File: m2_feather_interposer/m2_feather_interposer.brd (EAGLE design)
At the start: 160 x 186.6 mm, 43 parts, among them U1 MAX17043, U2 BQ24195, U3 XCL223

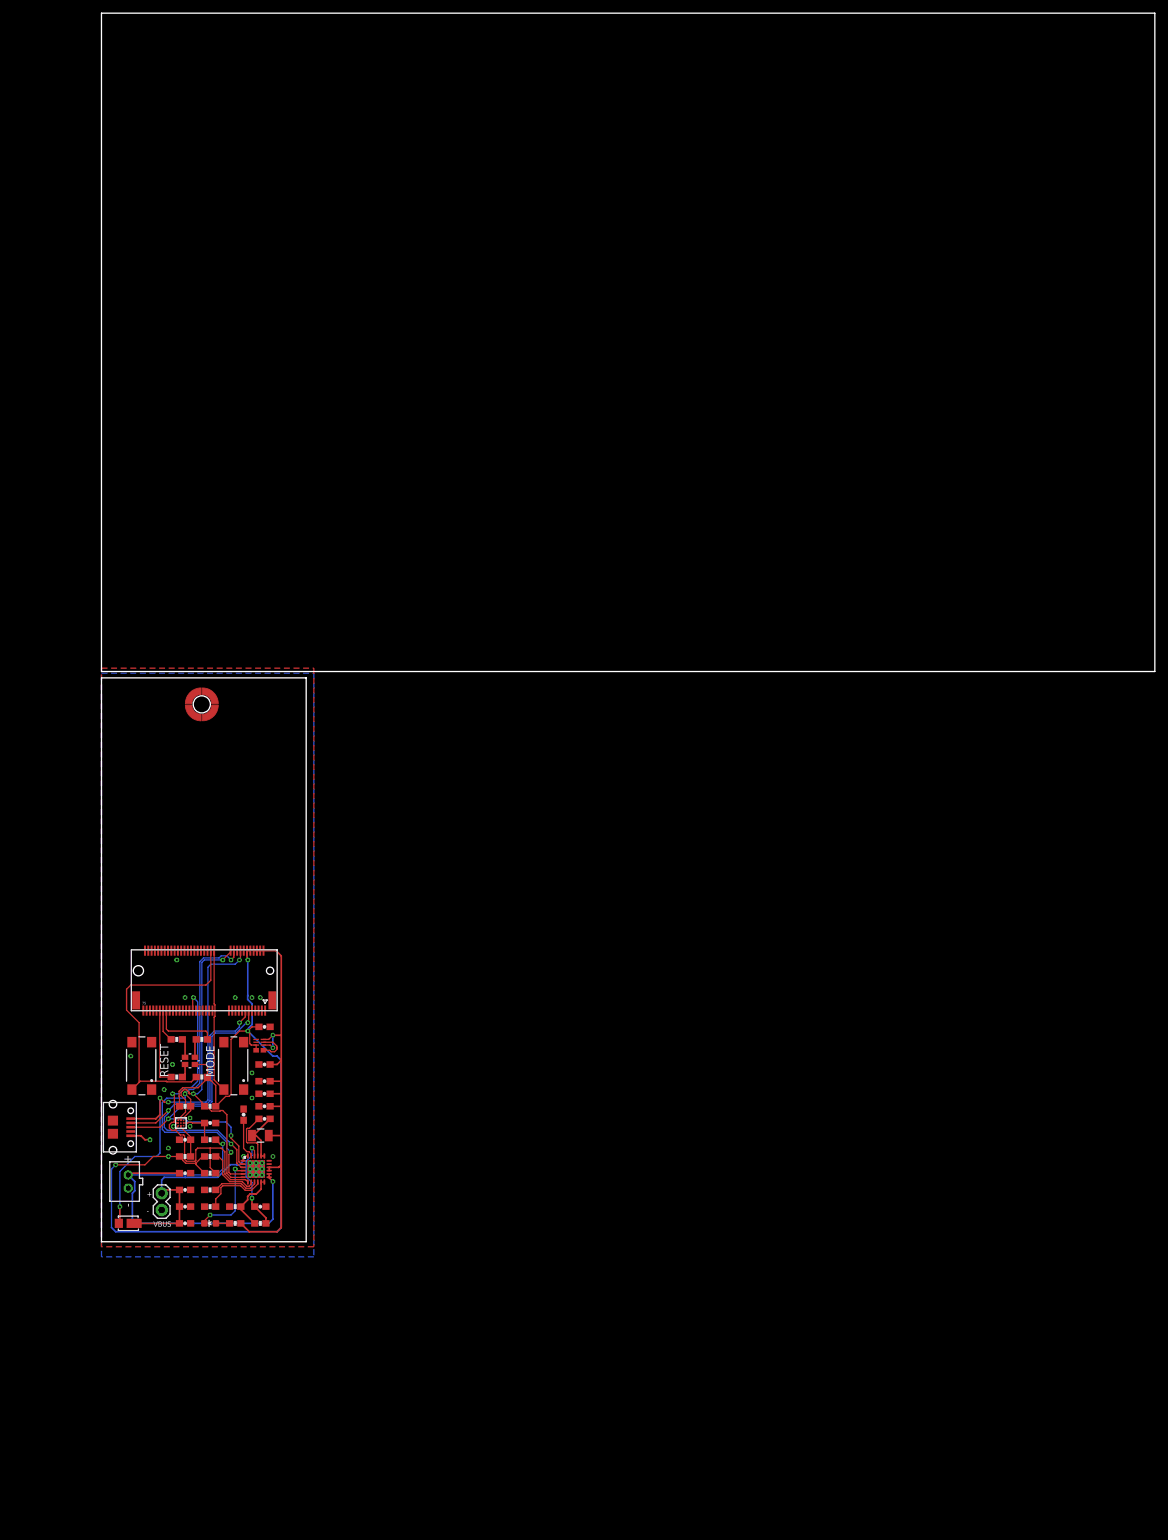
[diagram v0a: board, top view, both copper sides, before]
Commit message: added a whole bunch of stuff, board layout, draft key component placements, added connectors, added components from the boron that were missing.
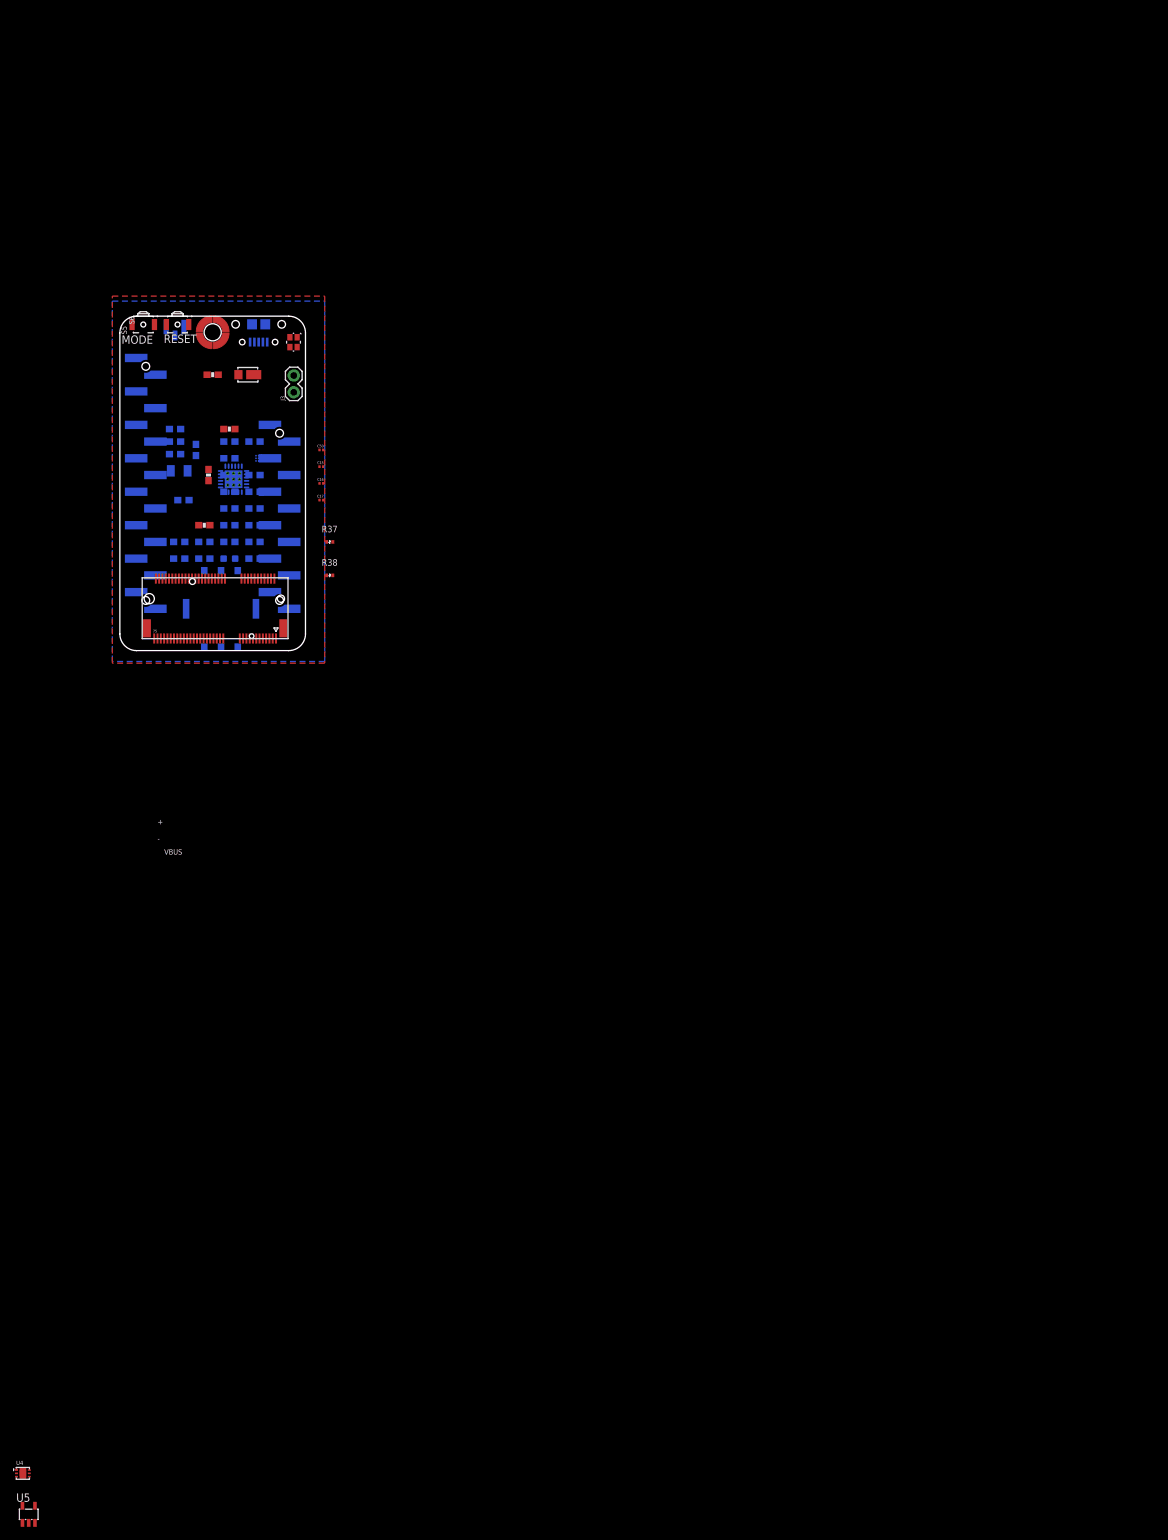
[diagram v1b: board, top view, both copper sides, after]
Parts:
- removed C13: 4.7uF, rickk2:0603-CAP
- removed C14: 10uF, rickk2:0603-CAP
- removed CN1: (no value), rickk2:JST-PH-2-THM
- removed JP1: M02PTH, rickk2:1X02
- removed S1, S2: SWITCH-MOM-4.5, rickk2:SWITCH-MOM-4.5
- removed U3: XCL223, rickk2:REG-XCL223-LESS-CREAM
- added C15, C16, C17: 47pF, m2_feather_interposer:PARTICLE_C0201_B
- added C50: 100nF, m2_feather_interposer:PARTICLE_C0201_B
- added J3: (no value), SparkFun-Connectors:1X02
- added MS1: MICROBUILDER_FEATHERWINGSMT_BTM_FEATHER, m2_feather_interposer:SMT_BTM_FEATHERWING
- added NFC: UFL, m2_feather_interposer:PARTICLE_IPEX-20279-001E
- added R37, R38: ESD NC, m2_feather_interposer:REDBEAR_R-0402S
- added S5, S6: B3U-3000P-B, m2_feather_interposer:SW_B3U-3000P-B
- added U$4: M2_FEATHER_INTERPOSER_PARTICLE_SIM-NANO-4FF, m2_feather_interposer:M2_FEATHER_INTERPOSER_PARTICLE_GCT-SIM8100
- added U4: PARTICLE_XC9258A33EER-G, m2_feather_interposer:PARTICLE_USP-6C
- added U5: PARTICLE_XC8107SOT25, m2_feather_interposer:PARTICLE_SOT25
- C1, C10, C11, C12, C4, C5, C6, C7, C8, C9: device rickk2:0603-CAP -> m2_feather_interposer:RICKK2_0603-CAP
- D1: device rickk2:LED-0603 -> m2_feather_interposer:RICKK2_LED-0603
- D2: device rickk2:SOD-123HE-ON -> m2_feather_interposer:RICKK2_SOD-123HE-ON
- J1: value (none) -> RICKK2_SPARK_M.2EKEY; device rickk2:SPARK_M.2EKEY-LESS-CREAM -> m2_feather_interposer:RICKK2_SPARK_M.2EKEY-LESS-CREAM
- L1: device rickk2:1008-BOURNS -> m2_feather_interposer:RICKK2_1008-BOURNS
- LED1: value LED-RGB-CREE-SMD -> RICKK2_LED-RGB-CREE-SMD; device rickk2:LED-RGB-CREE-SMD -> m2_feather_interposer:RICKK2_LED-RGB-CREE-SMD
- R1, R10, R11, R12, R14, R15, R2, R3, R4, R5, R6, R7, R8, R9: device rickk2:0603-RES -> m2_feather_interposer:RICKK2_0603-RES
- U$1: value M2-STANDOFF -> RICKK2_M2-STANDOFF; device rickk2:M2-STANDOFF -> m2_feather_interposer:RICKK2_M2-STANDOFF
- U$3: value USB-MICRO-B-SOCKET-AMPHENOL -> RICKK2_USB-MICRO-B-SOCKET-AMPHENOL; device rickk2:USB-B-SMT-AMPHENOL -> m2_feather_interposer:RICKK2_USB-B-SMT-AMPHENOL
- U1: device rickk2:9UCSP-MAXIM -> m2_feather_interposer:RICKK2_9UCSP-MAXIM
- U2: device rickk2:24VFQN-TI -> m2_feather_interposer:RICKK2_24VFQN-TI
- moved D2 130.2 mm to (22.2, 45.1)
- moved U$3 120.8 mm to (23.9, 50.0), flipped to the bottom, turned to 180 degrees
- moved LED1 110.3 mm to (29.7, 49.3), turned to 90 degrees
- moved U2 104.8 mm to (20.1, 29.2), flipped to the bottom
- moved C10 101.9 mm to (11.2, 36.8), flipped to the bottom
- moved C11 101.9 mm to (11.2, 34.9), flipped to the bottom
- moved C12 101.9 mm to (11.2, 33.0), flipped to the bottom
- moved C8 101.7 mm to (11.8, 19.7), flipped to the bottom
- moved R14 101.7 mm to (11.8, 17.1), flipped to the bottom
- moved U1 101.7 mm to (23.9, 32.4), flipped to the bottom
- moved C1 101.5 mm to (23.2, 29.8), flipped to the bottom
- moved C2 101.5 mm to (23.2, 19.7), flipped to the bottom
- moved C6 101.5 mm to (23.2, 22.2), flipped to the bottom
- moved C7 101.5 mm to (23.2, 24.8), flipped to the bottom
- moved R5 101.5 mm to (23.2, 27.3), flipped to the bottom
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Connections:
- removed net L2: U3.5, U3.8
- new net A0: J1.23, MS1.5
- new net A1: J1.33, MS1.6
- new net A2: J1.35, MS1.7
- new net A3: J1.37, MS1.8
- new net A4: J1.41, MS1.9
- new net A5: J1.43, MS1.10
- new net D2: MS1.19
- new net D3: MS1.20
- new net D4: MS1.21
- new net D5: MS1.22
- new net D6: MS1.23
- new net D7: MS1.24
- new net D8: MS1.25
- new net MISO: J1.50, MS1.13
- new net MOSI: J1.52, MS1.12
- new net NANO_CLK: C16.1
- new net NANO_DATA: C17.1
- new net NANO_RST: C15.1
- new net NANO_VSIM: C50.1
- new net NFC1: NFC.2@1, NFC.2@2, R37.1
- new net NFC2: NFC.1, R38.2
- new net RX: J1.38, MS1.14
- new net SCK: J1.54, MS1.11
- new net SYS_PWR_EN: MS1.27, U5.4
- new net TX: J1.36, MS1.15
- new net VOUT: U4.3, U5.1
- net /MODE: now also MS1.3, S5.2; no longer S1.3
- net /RESET: now also MS1.1, S6.2; no longer S2.3
- net 3V3: now also MS1.2; no longer C14.1, U3.3, U3.7
- net 3V7: now also U4.6; no longer C13.1, U3.4, U3.6
- net BAT: now also J3.1, MS1.28; no longer CN1.1
- net GND: now also C15.2, C16.2, C17.2, C50.2, J3.2, MS1.4, R37.2, R38.1, S5.1, S6.1, U4.2, U4.5, U4.P$1, U5.2; no longer C13.2, C14.2, CN1.2, JP1.2, S1.2, S2.2, U3.1, U3.2
- net SCL: now also MS1.18
- net SDA: now also MS1.17
- net VBUS: now also MS1.26, U5.5; no longer JP1.1
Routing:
- net 3V3: track 135.5 -> 0.00 mm, vias 4 -> 0
- net 3V7: track 70.6 -> 0.00 mm, vias 2 -> 0
- net VUSB: track 65.4 -> 0.00 mm, vias 4 -> 0
- net BAT: track 64.0 -> 0.00 mm, vias 2 -> 0
- net SCL: track 59.7 -> 0.00 mm, vias 3 -> 0
- net BATINT: track 52.4 -> 0.00 mm, vias 2 -> 0
- net SDA: track 51.8 -> 0.00 mm, vias 2 -> 0
- net USB-D-: track 49.7 -> 0.00 mm, vias 3 -> 0
- net USB-D+: track 48.7 -> 0.00 mm, vias 3 -> 0
- net /RESET: track 43.4 -> 0.00 mm
- net VBUS: track 32.6 -> 0.00 mm, vias 1 -> 0
- net /MODE: track 21.8 -> 0.00 mm
- net REGN: track 14.4 -> 0.00 mm, vias 2 -> 0
- net STAT: track 13.4 -> 0.00 mm, vias 2 -> 0
- net LED-B: track 11.8 -> 0.00 mm
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- added copper zone on layer 15, net GND
- added copper zone on layer 2, net GND
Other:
- board size 160 x 186.6 mm -> 28.2 x 50.8 mm

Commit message: all components added and key component placement done, driving through layout draft
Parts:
- removed U1: MAX17043, m2_feather_interposer:RICKK2_9UCSP-MAXIM
- removed U4: PARTICLE_XC9258A33EER-G, m2_feather_interposer:PARTICLE_USP-6C
- removed U5: PARTICLE_XC8107SOT25, m2_feather_interposer:PARTICLE_SOT25
- added C18, C19: 10uF/10V, rcl:C0603K
- added C20: 100nF, rcl:C0603K
- added C21: 100nF, Particle:C0201_B
- added D3: P1.03, SparkFun-LED:LED-0603
- added L2: 4.7uH, Particle:INDUCTOR-VLS-E
- added R11_, R16: 10K, adafruit:R0402
- added R13_: 332, adafruit:R0402
- added R17: 100k, adafruit:R0402
- added R19: 1K, Particle:C0201_B
- added U3: MAX1704X, SparkFun-IC-Power:TDFN-8
- added U6: XC9258A33EER-G, Particle:USP-6C
- added U7: XC8107SOT25, Particle:SOT25
- C1, C11, C12: device m2_feather_interposer:RICKK2_0603-CAP -> adafruit:C0402
- C3: device rickk2:0603-CAP -> adafruit:C0402
- R1, R10, R12, R14, R15, R5, R7, R8, R9: device m2_feather_interposer:RICKK2_0603-RES -> adafruit:R0402
- R11: value 10K -> 0; device m2_feather_interposer:RICKK2_0603-RES -> adafruit:R0402
- R13: value 332 -> 0; device rickk2:0603-RES -> adafruit:R0402
- R2, R3, R4: value 1K -> 1k; device m2_feather_interposer:RICKK2_0603-RES -> adafruit:R0402
- R6: value 1K -> 4.7K; device m2_feather_interposer:RICKK2_0603-RES -> adafruit:R0402
- moved LED1 50.6 mm to (5.08, 5.08)
- moved S6 50.4 mm to (26.5, 4.57), flipped to the bottom, turned to 180 degrees
- moved S5 48.2 mm to (8.51, 4.57), flipped to the bottom, turned to 180 degrees
- moved R38 46.1 mm to (8.00, 52.2), flipped to the bottom, turned to 270 degrees
- moved R3 41.9 mm to (4.83, 4.95), flipped to the bottom, turned to 0 degrees
- moved R37 39.2 mm to (12.8, 52.2), flipped to the bottom, turned to 90 degrees
- moved D1 37.9 mm to (5.21, 52.3), flipped to the top, turned to 0 degrees
- moved R12 36.4 mm to (5.33, 52.1), turned to 90 degrees
- moved R13 33.4 mm to (25.1, 52.6), turned to 270 degrees
- moved R4 30.9 mm to (5.21, 9.40), turned to 90 degrees
- moved R11 30.7 mm to (23.7, 52.6), turned to 270 degrees
- moved C17 29.2 mm to (11.6, 6.73), flipped to the bottom, turned to 270 degrees
- moved R7 27.5 mm to (29.6, 9.40), flipped to the top, turned to 90 degrees
- moved R14 27.0 mm to (17.9, 43.4)
- moved R15 25.1 mm to (17.9, 44.7), turned to 180 degrees
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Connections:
- removed net VOUT: U4.3, U5.1
- new net N$23: R16.2, U6.4
- new net N$24: D3.C, R19.2
- new net N$25: L2.P$1, U6.1
- new net N$4: R11.1, U$3.3
- new net N$8: R13.1, U$3.2
- new net PMIC_VSYS: C10.1, C11.1, C9.1, L1.2, R12.2, R17.2, U2.15, U2.16, U7.5
- new net USB_D_N: J1.13, R13.2
- new net USB_D_P: J1.11, R11.2
- net 3V3: now also C19.1, C21.1, L2.P$2, U6.3
- net 3V7: now also C18.1, C20.1, R16.1, U6.6, U7.1; no longer C10.1, C11.1, C9.1, L1.2, R12.2, U2.15, U2.16, U4.6
- net BATINT: now also U3.5; no longer U1.C1
- net BQCE: now also R11_.2; no longer R11.2
- net D2: now also J1.40
- net D3: now also J1.42
- net D4: now also J1.66
- net D5: now also J1.68
- net D6: now also J1.70
- net D7: now also D3.A, J1.72
- net D8: now also J1.48
- net GND: now also C18.2, C19.2, C20.2, C21.2, R11_.1, R13_.1, R19.1, U$4.C5, U3.1, U3.4, U3.6, U3.EP, U6.2, U6.5, U6.P$1, U7.2; no longer R11.1, R13.1, U1.A3, U1.B1, U1.C3, U4.2, U4.5, U4.P$1, U5.2
- net ILIM: now also R13_.2; no longer R13.2
- net N$3: now also U3.2; no longer U1.B3
- net N$5: now also U3.3; no longer U1.C2
- net NANO_CLK: now also J1.71, U$4.C3
- net NANO_DATA: now also J1.73, U$4.C7
- net NANO_RST: now also J1.69, U$4.C2
- net NANO_VSIM: now also J1.67, U$4.C1
- net NFC1: now also J1.17
- net NFC2: now also J1.19
- net SCL: now also U3.7; no longer U1.A2
- net SDA: now also U3.8; no longer U1.A1
- net SYS_PWR_EN: now also R17.1, U7.4; no longer U5.4
- net USB-D+: no longer J1.11, U$3.3
- net USB-D-: no longer J1.13, U$3.2
- net VBUS: no longer U5.5
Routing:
- net 3V3: track 0.00 -> 41.4 mm, vias 0 -> 1
- net SDA: track 0.00 -> 15.0 mm, vias 0 -> 1
- net SCL: track 0.00 -> 12.5 mm, vias 0 -> 1
- net A1: track 0.00 -> 11.6 mm, vias 0 -> 1
- net TX: track 0.00 -> 10.8 mm
- net RX: track 0.00 -> 9.95 mm
- net A2: track 0.00 -> 9.69 mm, vias 0 -> 1
- net A4: track 0.00 -> 9.68 mm, vias 0 -> 1
- net NANO_DATA: track 0.00 -> 8.14 mm
- net A0: track 0.00 -> 8.10 mm, vias 0 -> 1
- net A5: track 0.00 -> 7.04 mm, vias 0 -> 1
- net /RESET: track 0.00 -> 6.26 mm, vias 0 -> 1
- net /MODE: track 0.00 -> 5.52 mm, vias 0 -> 1
- net LED-G: track 0.00 -> 4.62 mm
- net D8: track 0.00 -> 4.50 mm, vias 0 -> 1
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- added copper zone on layer 1, net 3V3
- added copper zone on layer 1, net 3V7
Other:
- board size 28.2 x 50.8 mm -> 28.2 x 53.6 mm
- board text removed: "SomTest1 v4"
